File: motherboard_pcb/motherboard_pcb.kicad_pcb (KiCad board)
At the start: 2 copper layers, 6 parts, among them J1 Conn_01x04_Socket, U1 ESP32-DEVKIT-V1

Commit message: Added shift registers to the skematic and started attempting to route
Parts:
- added C1: 100µF, Capacitor_THT:CP_Radial_D5.0mm_P2.50mm, F.Cu at (113.0, 64.7)
- added C2: 100µF, Capacitor_THT:CP_Radial_D5.0mm_P2.50mm, F.Cu at (113.0, 90.2)
- added C3: 100µF, Capacitor_THT:CP_Radial_D5.0mm_P2.50mm, F.Cu at (104.2, 103.9)
- added C4: 100µF, Capacitor_THT:CP_Radial_D5.0mm_P2.50mm, F.Cu at (104.2, 110.5)
- added D1: LED, LED_THT:LED_D3.0mm, F.Cu at (113.0, 47.0)
- added D2: LED, LED_THT:LED_D3.0mm, F.Cu at (113.5, 72.5)
- added D3: LED, LED_THT:LED_D3.0mm, F.Cu at (160.4, 127.4)
- added D4: LED, LED_THT:LED_D3.0mm, F.Cu at (160.4, 132.9)
- added J6: OLED Display I2C, Connector_PinSocket_2.54mm:PinSocket_1x04_P2.54mm_Vertical, F.Cu at (80.0, 99.1)
- added Mot1: Conn_01x04_Socket, Connector_JST:JST_PH_B4B-PH-K_1x04_P2.00mm_Vertical, F.Cu at (113.0, 51.9)
- added Mot2: Conn_01x04_Socket, Connector_JST:JST_PH_B4B-PH-K_1x04_P2.00mm_Vertical, F.Cu at (113.5, 77.5)
- added Mot3: Conn_01x04_Socket, Connector_JST:JST_PH_B4B-PH-K_1x04_P2.00mm_Vertical, F.Cu at (149.7, 128.5)
- added Mot4: Conn_01x04_Socket, Connector_JST:JST_PH_B4B-PH-K_1x04_P2.00mm_Vertical, F.Cu at (149.7, 135.1)
- added R1: 65, Resistor_THT:R_Axial_DIN0207_L6.3mm_D2.5mm_P10.16mm_Horizontal, F.Cu at (107.5, 57.1)
- added R2: 65, Resistor_THT:R_Axial_DIN0207_L6.3mm_D2.5mm_P10.16mm_Horizontal, F.Cu at (148.3, 140.9)
- added R2: 65, Resistor_THT:R_Axial_DIN0207_L6.3mm_D2.5mm_P10.16mm_Horizontal, F.Cu at (107.5, 82.7)
- added R3: 65, Resistor_THT:R_Axial_DIN0207_L6.3mm_D2.5mm_P10.16mm_Horizontal, F.Cu at (148.3, 144.9)
- added R3: 65, Resistor_THT:R_Axial_DIN0207_L6.3mm_D2.5mm_P10.16mm_Horizontal, F.Cu at (85.8, 92.5)
- added R4: 65, Resistor_THT:R_Axial_DIN0207_L6.3mm_D2.5mm_P10.16mm_Horizontal, F.Cu at (148.3, 149.0)
- added R4: 65, Resistor_THT:R_Axial_DIN0207_L6.3mm_D2.5mm_P10.16mm_Horizontal, F.Cu at (85.8, 96.5)
- added Sft1: 74HC596, Package_DIP:DIP-16_W7.62mm, F.Cu at (138.4, 48.4)
- added Sft2: 74HC596, Package_DIP:DIP-16_W7.62mm, F.Cu at (138.5, 73.6)
- added Sft3: 74HC596, Package_DIP:DIP-16_W7.62mm, F.Cu at (126.8, 121.3)
- added Sft4: 74HC596, Package_DIP:DIP-16_W7.62mm, F.Cu at (137.6, 121.3)
- A1, A2, A3, A4: value Pololu_Breakout_DRV8825 -> Drv1
- J1: value Conn_01x04_Socket -> 12 Power Supply Input; footprint Connector_JST:JST_PH_B4B-PH-K_1x04_P2.00mm_Vertical -> TerminalBlock:TerminalBlock_Xinya_XY308-2.54-2P_1x02_P2.54mm_Horizontal
- moved A3 129.4 mm to (119.7, 96.6)
- moved U1 122.1 mm to (48.7, 106.1)
- moved A2 115.8 mm to (119.7, 71.1)
- moved A4 115.7 mm to (150.1, 99.4)
- moved A1 109.5 mm to (119.4, 45.7)
- moved J1 70.3 mm to (113.0, 21.6), turned to 180 degrees
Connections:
- A1 pad 10: unconnected-(A1-M0-Pad10) -> Net-(A1-M0)
- A1 pad 11: unconnected-(A1-M1-Pad11) -> Net-(A1-M1)
- A1 pad 12: unconnected-(A1-M2-Pad12) -> Net-(A1-M2)
- A1 pad 13: unconnected-(A1-~{RST}-Pad13) -> Net-(A1-~{RST})
- A1 pad 14: unconnected-(A1-~{SLP}-Pad14) -> Net-(A1-~{SLP})
- A1 pad 15: unconnected-(A1-STEP-Pad15) -> STP1
- A1 pad 16: unconnected-(A1-DIR-Pad16) -> Net-(A1-DIR)
- A1 pad 2: unconnected-(A1-~{FLT}-Pad2) -> Net-(A1-~{FLT})
- A1 pad 3: unconnected-(A1-A2-Pad3) -> Net-(A1-A2)
- A1 pad 4: unconnected-(A1-A1-Pad4) -> Net-(A1-A1)
- A1 pad 5: unconnected-(A1-B1-Pad5) -> Net-(A1-B1)
- A1 pad 6: unconnected-(A1-B2-Pad6) -> Net-(A1-B2)
- A1 pad 7: GNDPWR -> -12V
- A1 pad 8: unconnected-(A1-VMOT-Pad8) -> +12V
- A1 pad 9: unconnected-(A1-~{EN}-Pad9) -> Net-(A1-~{EN})
- A2 pad 10: unconnected-(A2-M0-Pad10) -> Net-(A2-M0)
- A2 pad 11: unconnected-(A2-M1-Pad11) -> Net-(A2-M1)
- A2 pad 12: unconnected-(A2-M2-Pad12) -> Net-(A2-M2)
- A2 pad 13: unconnected-(A2-~{RST}-Pad13) -> Net-(A2-~{RST})
- A2 pad 14: unconnected-(A2-~{SLP}-Pad14) -> Net-(A2-~{SLP})
- A2 pad 15: unconnected-(A2-STEP-Pad15) -> STP1
- A2 pad 16: unconnected-(A2-DIR-Pad16) -> Net-(A2-DIR)
- A2 pad 2: unconnected-(A2-~{FLT}-Pad2) -> Net-(A2-~{FLT})
- A2 pad 3: unconnected-(A2-A2-Pad3) -> Net-(A2-A2)
- A2 pad 4: unconnected-(A2-A1-Pad4) -> Net-(A2-A1)
- A2 pad 5: unconnected-(A2-B1-Pad5) -> Net-(A2-B1)
- A2 pad 6: unconnected-(A2-B2-Pad6) -> Net-(A2-B2)
- A2 pad 7: GNDPWR -> -12V
- A2 pad 8: unconnected-(A2-VMOT-Pad8) -> +12V
- A2 pad 9: unconnected-(A2-~{EN}-Pad9) -> Net-(A2-~{EN})
- A3 pad 10: unconnected-(A3-M0-Pad10) -> Net-(A3-M0)
- A3 pad 11: unconnected-(A3-M1-Pad11) -> Net-(A3-M1)
- A3 pad 12: unconnected-(A3-M2-Pad12) -> Net-(A3-M2)
- A3 pad 13: unconnected-(A3-~{RST}-Pad13) -> Net-(A3-~{RST})
- A3 pad 14: unconnected-(A3-~{SLP}-Pad14) -> Net-(A3-~{SLP})
- A3 pad 15: unconnected-(A3-STEP-Pad15) -> STP1
- A3 pad 16: unconnected-(A3-DIR-Pad16) -> Net-(A3-DIR)
- A3 pad 2: unconnected-(A3-~{FLT}-Pad2) -> Net-(A3-~{FLT})
- A3 pad 3: unconnected-(A3-A2-Pad3) -> Net-(A3-A2)
- A3 pad 4: unconnected-(A3-A1-Pad4) -> Net-(A3-A1)
- A3 pad 5: unconnected-(A3-B1-Pad5) -> Net-(A3-B1)
- A3 pad 6: unconnected-(A3-B2-Pad6) -> Net-(A3-B2)
- A3 pad 7: GNDPWR -> -12V
- A3 pad 8: unconnected-(A3-VMOT-Pad8) -> +12V
- A3 pad 9: unconnected-(A3-~{EN}-Pad9) -> Net-(A3-~{EN})
- A4 pad 1: unconnected-(A4-GND-Pad1) -> GND
- A4 pad 10: unconnected-(A4-M0-Pad10) -> Net-(A4-M0)
- A4 pad 11: unconnected-(A4-M1-Pad11) -> Net-(A4-M1)
- A4 pad 12: unconnected-(A4-M2-Pad12) -> Net-(A4-M2)
- A4 pad 13: unconnected-(A4-~{RST}-Pad13) -> Net-(A4-~{RST})
- A4 pad 14: unconnected-(A4-~{SLP}-Pad14) -> Net-(A4-~{SLP})
- A4 pad 15: unconnected-(A4-STEP-Pad15) -> STP1
- A4 pad 16: unconnected-(A4-DIR-Pad16) -> Net-(A4-DIR)
- A4 pad 2: unconnected-(A4-~{FLT}-Pad2) -> Net-(A4-~{FLT})
- A4 pad 3: unconnected-(A4-A2-Pad3) -> Net-(A4-A2)
- A4 pad 4: unconnected-(A4-A1-Pad4) -> Net-(A4-A1)
- A4 pad 5: unconnected-(A4-B1-Pad5) -> Net-(A4-B1)
- A4 pad 6: unconnected-(A4-B2-Pad6) -> Net-(A4-B2)
- A4 pad 7: GNDPWR -> -12V
- A4 pad 8: unconnected-(A4-VMOT-Pad8) -> +12V
- A4 pad 9: unconnected-(A4-~{EN}-Pad9) -> Net-(A4-~{EN})
- J1 pad 1: unconnected-(J1-Pin_1-Pad1) -> -12V
- J1 pad 2: unconnected-(J1-Pin_2-Pad2) -> +12V
- U1 pad 11: unconnected-(U1-D21-Pad11) -> I2C_SDA
- U1 pad 14: unconnected-(U1-D22-Pad14) -> I2C_SCL
- U1 pad 25: unconnected-(U1-D27-Pad25) -> RCLK
- U1 pad 26: unconnected-(U1-D14-Pad26) -> SRCLR
- U1 pad 27: unconnected-(U1-D12-Pad27) -> SRCLK
- U1 pad 28: unconnected-(U1-D13-Pad28) -> OE
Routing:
- net GND: track 0.00 -> 115.7 mm
- net SRCLK: track 0.00 -> 31.6 mm
- net RCLK: track 0.00 -> 31.3 mm
- net Net-(Sft1-QH'): track 0.00 -> 15.9 mm
- net STP1: track 0.00 -> 15.5 mm
- net -12V: track 0.00 -> 14.1 mm
- net +12V: track 0.00 -> 14.1 mm
- net Net-(A1-DIR): track 0.00 -> 7.46 mm
- net Net-(A2-DIR): track 0.00 -> 7.27 mm
- net Net-(A1-~{FLT}): track 0.00 -> 6.89 mm
- net Net-(A1-A2): track 0.00 -> 6.81 mm
- net Net-(A2-A2): track 0.00 -> 6.70 mm
- net Net-(A1-A1): track 0.00 -> 6.68 mm
- net Net-(A2-~{FLT}): track 0.00 -> 6.60 mm
- net Net-(A1-B2): track 0.00 -> 6.58 mm
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
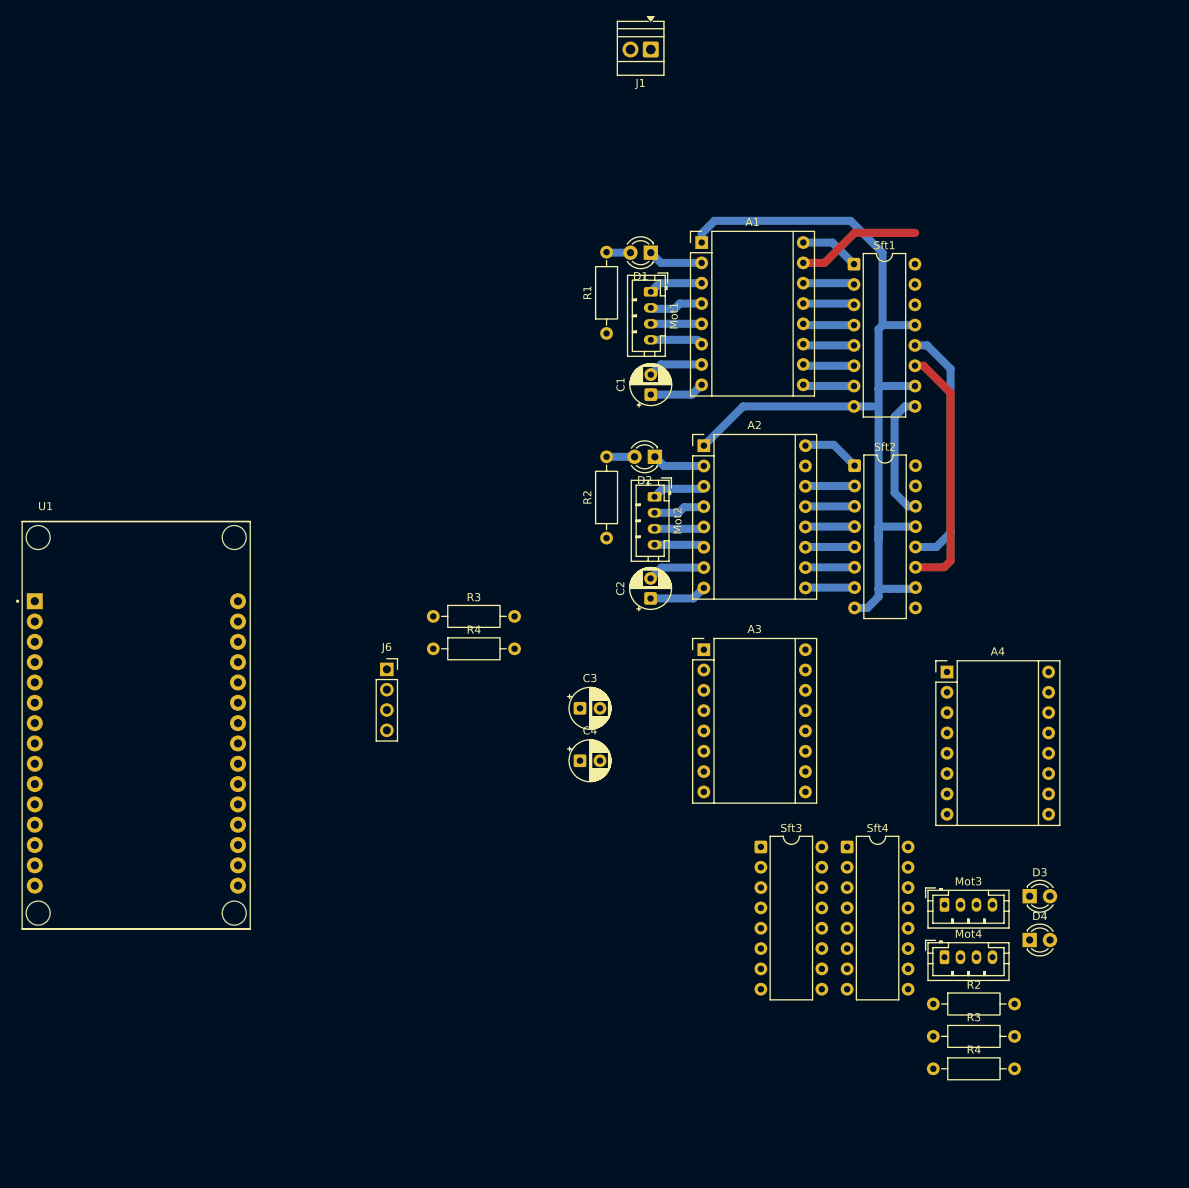
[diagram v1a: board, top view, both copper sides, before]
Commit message: Most of the motor stuff has been routed
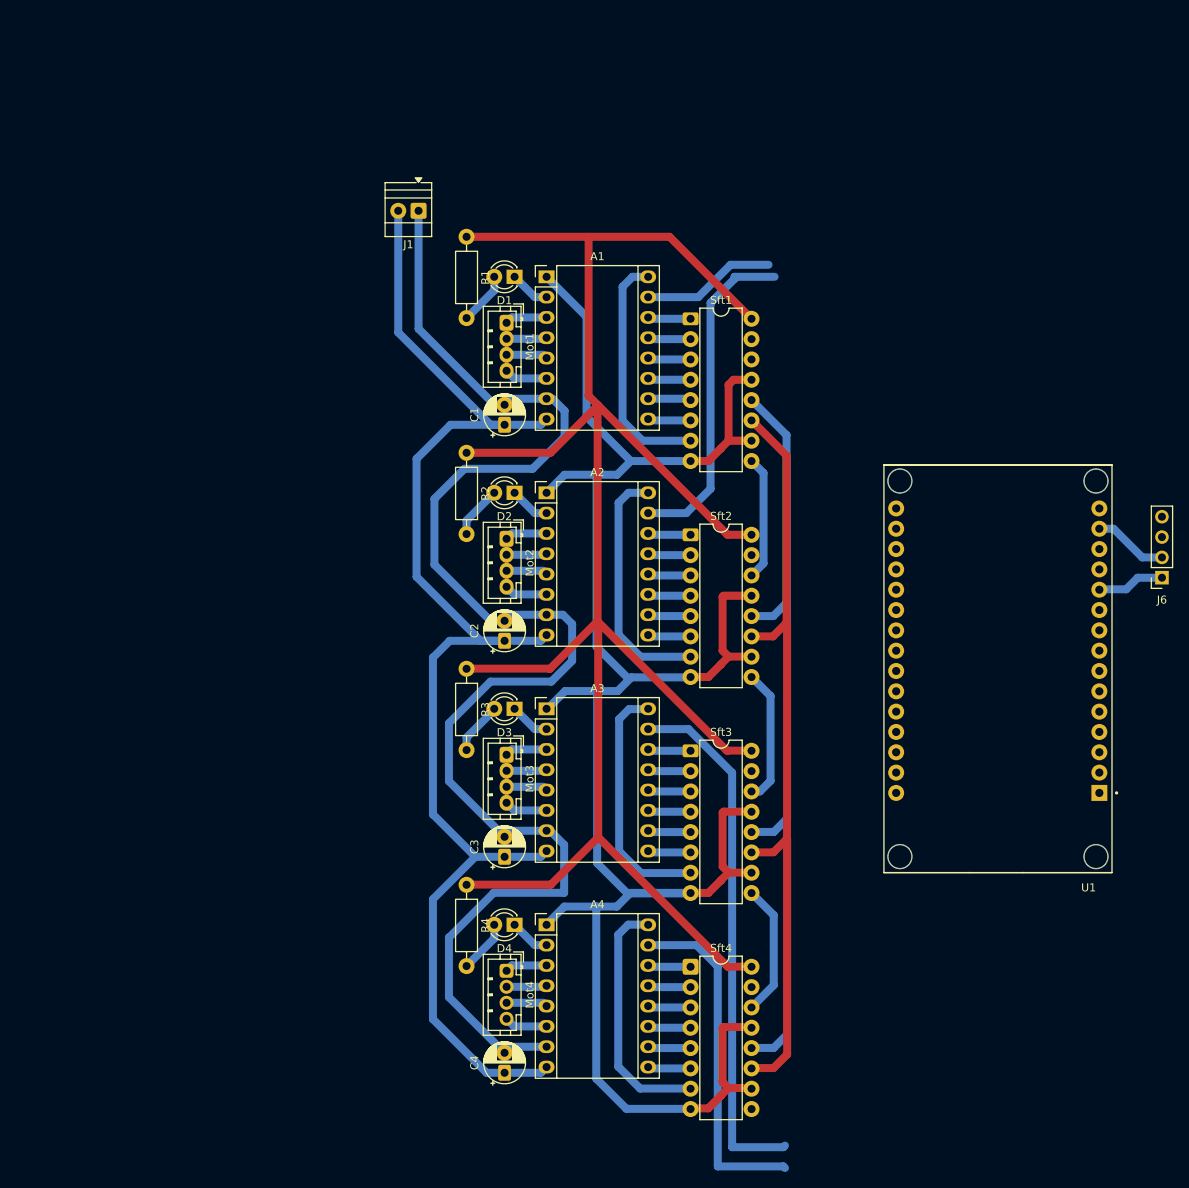
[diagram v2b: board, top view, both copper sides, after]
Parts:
- removed the R2 at (148.3, 140.9)
- removed the R2 at (107.5, 82.7)
- removed the R3 at (148.3, 144.9)
- removed the R3 at (85.8, 92.5)
- removed the R4 at (148.3, 149.0)
- removed the R4 at (85.8, 96.5)
- added R2: 65, Resistor_THT:R_Axial_DIN0207_L6.3mm_D2.5mm_P10.16mm_Horizontal, F.Cu at (90.0, 72.0)
- added R3: 65, Resistor_THT:R_Axial_DIN0207_L6.3mm_D2.5mm_P10.16mm_Horizontal, F.Cu at (90.0, 99.0)
- added R4: 65, Resistor_THT:R_Axial_DIN0207_L6.3mm_D2.5mm_P10.16mm_Horizontal, F.Cu at (90.0, 126.0)
- moved U1 107.9 mm to (156.4, 99.0), turned to 180 degrees
- moved J6 97.6 mm to (176.9, 87.6), turned to 180 degrees
- moved D3 68.5 mm to (96.0, 104.0), turned to 180 degrees
- moved D4 64.4 mm to (96.0, 131.0), turned to 180 degrees
- moved A4 59.2 mm to (100.0, 131.0)
- moved Mot3 57.9 mm to (95.0, 109.8), turned to -90 degrees
- moved Mot4 54.8 mm to (95.0, 136.8), turned to -90 degrees
- moved C4 40.1 mm to (94.8, 149.5), turned to 90 degrees
- moved J1 35.3 mm to (84.0, 41.8)
- moved Sft4 24.6 mm to (118.0, 136.2)
- moved Sft2 22.2 mm to (118.0, 82.2)
- moved Sft1 21.5 mm to (118.0, 55.2)
- moved R1 21.3 mm to (90.0, 45.0), turned to -90 degrees
- moved A3 21.0 mm to (100.0, 104.0)
- moved C3 20.8 mm to (94.8, 122.5), turned to 90 degrees
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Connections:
- A1 pad 10: Net-(A1-M0) -> M1_M0
- A1 pad 11: Net-(A1-M1) -> M1_M1
- A1 pad 12: Net-(A1-M2) -> M1_M2
- A1 pad 13: Net-(A1-~{RST}) -> M1_RST
- A1 pad 14: Net-(A1-~{SLP}) -> M1_SLP
- A1 pad 16: Net-(A1-DIR) -> M1_DIR
- A1 pad 9: Net-(A1-~{EN}) -> M1_EN
- A2 pad 10: Net-(A2-M0) -> M2_M0
- A2 pad 11: Net-(A2-M1) -> M2_M1
- A2 pad 12: Net-(A2-M2) -> M2_M2
- A2 pad 13: Net-(A2-~{RST}) -> M2_RST
- A2 pad 14: Net-(A2-~{SLP}) -> M2_SLP
- A2 pad 15: STP1 -> STP2
- A2 pad 16: Net-(A2-DIR) -> M2_DIR
- A2 pad 9: Net-(A2-~{EN}) -> M2_EN
- A3 pad 10: Net-(A3-M0) -> M3_M0
- A3 pad 11: Net-(A3-M1) -> M3_M1
- A3 pad 12: Net-(A3-M2) -> M3_M2
- A3 pad 13: Net-(A3-~{RST}) -> M3_RST
- A3 pad 14: Net-(A3-~{SLP}) -> M3_SLP
- A3 pad 15: STP1 -> STP3
- A3 pad 16: Net-(A3-DIR) -> M3_DIR
- A3 pad 9: Net-(A3-~{EN}) -> M3_EN
- A4 pad 10: Net-(A4-M0) -> M4_M0
- A4 pad 11: Net-(A4-M1) -> M4_M1
- A4 pad 12: Net-(A4-M2) -> M4_M2
- A4 pad 13: Net-(A4-~{RST}) -> M4_RST
- A4 pad 14: Net-(A4-~{SLP}) -> M4_SLP
- A4 pad 15: STP1 -> STP4
- A4 pad 16: Net-(A4-DIR) -> M4_DIR
- A4 pad 9: Net-(A4-~{EN}) -> M4_EN
- Sft1 pad 1: Net-(A1-DIR) -> M1_SLP
- Sft1 pad 14: unconnected-(Sft1-SER-Pad14) -> SER
- Sft1 pad 2: Net-(A1-~{SLP}) -> M1_RST
- Sft1 pad 3: Net-(A1-~{RST}) -> M1_M2
- Sft1 pad 4: Net-(A1-M2) -> M1_M1
- Sft1 pad 5: Net-(A1-M1) -> M1_M0
- Sft1 pad 6: Net-(A1-M0) -> M1_EN
- Sft1 pad 7: Net-(A1-~{EN}) -> M1_DIR
- Sft2 pad 1: Net-(A2-DIR) -> M2_SLP
- Sft2 pad 2: Net-(A2-~{SLP}) -> M2_RST
- Sft2 pad 3: Net-(A2-~{RST}) -> M2_M2
- Sft2 pad 4: Net-(A2-M2) -> M2_M1
- Sft2 pad 5: Net-(A2-M1) -> M2_M0
- Sft2 pad 6: Net-(A2-M0) -> M2_EN
- Sft2 pad 7: Net-(A2-~{EN}) -> M2_DIR
- Sft3 pad 1: Net-(A3-DIR) -> M3_SLP
- Sft3 pad 2: Net-(A3-~{SLP}) -> M3_RST
- Sft3 pad 3: Net-(A3-~{RST}) -> M3_M2
- Sft3 pad 4: Net-(A3-M2) -> M3_M1
- Sft3 pad 5: Net-(A3-M1) -> M3_M0
- Sft3 pad 6: Net-(A3-M0) -> M3_EN
- Sft3 pad 7: Net-(A3-~{EN}) -> M3_DIR
- Sft4 pad 1: Net-(A4-DIR) -> M4_SLP
- Sft4 pad 2: Net-(A4-~{SLP}) -> M4_RST
- Sft4 pad 3: Net-(A4-~{RST}) -> M4_M2
- Sft4 pad 4: Net-(A4-M2) -> M4_M1
- Sft4 pad 5: Net-(A4-M1) -> M4_M0
- Sft4 pad 6: Net-(A4-M0) -> M4_EN
- Sft4 pad 7: Net-(A4-~{EN}) -> M4_DIR
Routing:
- net +3.3V: track 0.00 -> 249.8 mm
- net -12V: track 14.1 -> 184.1 mm
- net +12V: track 14.1 -> 172.1 mm
- net GND: track 115.7 -> 262.2 mm
- net STP3: track 0.00 -> 66.2 mm
- net RCLK: track 31.3 -> 96.4 mm
- net SRCLK: track 31.6 -> 96.4 mm
- net STP4: track 0.00 -> 43.3 mm
- net STP2: track 0.00 -> 41.8 mm
- net M3_DIR: track 0.00 -> 30.9 mm
- net M2_DIR: track 0.00 -> 30.9 mm
- net M4_DIR: track 0.00 -> 30.9 mm
- net M1_DIR: track 0.00 -> 30.0 mm
- net Net-(Sft2-QH'): track 0.00 -> 16.9 mm
- net Net-(Sft3-QH'): track 0.00 -> 16.6 mm
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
